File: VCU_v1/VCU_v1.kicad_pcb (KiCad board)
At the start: 4 copper layers, 265 parts, among them J1 Conn_01x04, J2 NUCLEO CONNECTOR LEFT, J3 NUCLEO CONNECTOR RIGHT, J4 Micro_SD_Card, J5 BRUHBus, J6 BRUHBus, J7 BRUHBus, J8 BRUHBus, Q1 PMOS, Q2 BSD235NH6327XT, Q3 SP8K80TB1, Q4 SP8K80TB1, Q5 SP8K80TB1, Q6 BSD235NH6327XT, SW1 SW_Push, U1 TPS5430, U10 TSB712AIDT, U11 MCP2562 E/SN, U12 MCP2562 E/SN, U13 TPA3116D2QDADRQ1, U14 PCM5102APWR, U2 TPS5430, U3 AMS1117-3.3, U4 MIC5200-4.8YS, U5 STM32H723ZGT6, U6 MX150 20-pin, U7 MX150 20-pin, U8 MX150 20-pin, U9 TSB712AIDT, Y1 16 MHz, Y2 32.768 kHz

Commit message: layout of power converters, connectors, nucleo headers
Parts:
- moved C14 289.5 mm to (341.1, 148.0)
- moved C15 289.5 mm to (341.1, 150.5)
- moved C16 289.5 mm to (341.1, 153.0)
- moved C17 289.5 mm to (341.1, 155.5)
- moved C26 289.5 mm to (441.7, 32.6)
- moved C27 289.5 mm to (441.7, 35.1)
- moved C28 289.5 mm to (441.7, 37.6)
- moved C29 289.5 mm to (441.7, 40.1)
- moved C30 289.5 mm to (441.7, 42.6)
- moved C31 289.5 mm to (441.7, 45.2)
- moved C32 289.5 mm to (441.7, 47.7)
- moved C33 289.5 mm to (441.7, 50.2)
- moved C45 289.5 mm to (353.8, 171.6)
- moved C46 289.5 mm to (353.8, 154.6)
- moved C55 289.5 mm to (468.7, 53.7)
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
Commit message: omids wisdom came all over my power converters
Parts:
- moved J7 420.7 mm to (34.0, 76.7), turned to 90 degrees
- moved J8 420.1 mm to (34.0, 98.0), turned to 90 degrees
- moved J4 367.5 mm to (32.1, 136.3), turned to 90 degrees
- moved U13 355.2 mm to (126.0, 71.3)
- moved U14 355.2 mm to (126.0, 87.4)
- moved H2 351.2 mm to (29.2, 57.1)
- moved L3 337.9 mm to (140.9, 74.5)
- moved L4 337.9 mm to (140.9, 88.2)
- moved H4 334.9 mm to (30.9, 170.7)
- moved U5 326.8 mm to (110.2, 138.0), turned to 90 degrees
- moved BT1 271.2 mm to (199.0, 147.1)
- moved TP1 196.9 mm to (212.5, 141.6)
- moved TP48 161.9 mm to (212.5, 137.4)
- moved H3 121.5 mm to (244.2, 168.5)
- moved L2 84.0 mm to (193.8, 118.9), turned to 0 degrees
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
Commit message: vcu placements complete
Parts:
- removed J5: BRUHBus, Connector_RJ:RJ45_Amphenol_RJHSE538X
- removed R33: 10k, Resistor_SMD:R_0603_1608Metric_Pad0.98x0.95mm_HandSolder
- removed R35: 100, Resistor_SMD:R_0603_1608Metric_Pad0.98x0.95mm_HandSolder
- removed R37, R39: 1.6k, Resistor_SMD:R_0603_1608Metric_Pad0.98x0.95mm_HandSolder
- D3, D4, D7: footprint LED_SMD:LED_0201_0603Metric_Pad0.64x0.40mm_HandSolder -> LED_SMD:LED_0603_1608Metric_Pad1.05x0.95mm_HandSolder
- U11, U12: value MCP2562 E/SN -> MCP2562FD-E/SN
- moved R79 431.7 mm to (43.7, 65.6), turned to -90 degrees
- moved R81 431.3 mm to (43.7, 76.5), turned to -90 degrees
- moved R80 430.5 mm to (43.7, 88.6), turned to -90 degrees
- moved R82 430.4 mm to (43.7, 98.0), turned to -90 degrees
- moved R78 424.0 mm to (47.2, 79.2), turned to 180 degrees
- moved R77 423.2 mm to (47.3, 86.4), turned to 180 degrees
- moved Q6 422.3 mm to (46.7, 82.8), turned to 90 degrees
- moved R10 421.0 mm to (37.8, 148.0), turned to -90 degrees
- moved R76 420.7 mm to (50.0, 80.1), turned to 90 degrees
- moved R75 420.2 mm to (50.0, 85.2), turned to -90 degrees
- moved C36 415.9 mm to (48.5, 154.8), turned to 90 degrees
- moved C32 412.4 mm to (42.2, 150.0)
- moved C37 411.8 mm to (52.1, 154.8), turned to 90 degrees
- moved C31 411.5 mm to (42.2, 143.6)
- moved C30 410.9 mm to (42.2, 138.5)
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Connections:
- Q2 pad 3: Net-(J6-CAN_IND) -> unconnected-(Q2B-D-Pad3)
- Q2 pad 4: GND -> unconnected-(Q2B-S-Pad4)
- Q2 pad 5: Net-(Q2B-G) -> unconnected-(Q2B-G-Pad5)
- Q2 pad 6: Net-(J5-CAN_IND) -> Net-(J6-CAN_IND)
- Q5 pad 1: /Connector-Root/BMS_FAULT- -> GND
- Q5 pad 3: /Connector-Root/IMD_FAULT- -> GND
- R36 pad 2: Net-(Q2B-G) -> Net-(Q2A-G)
- R60 pad 1: /Connector-Root/BMS_FAULT- -> GND
- R69 pad 1: /Connector-Root/IMD_FAULT- -> GND
- U6 pad 11: unconnected-(U6-Pad11) -> /BRUHbus/CAN1_L
- U6 pad 12: unconnected-(U6-Pad12) -> /BRUHbus/CAN1_H
- U6 pad 13: unconnected-(U6-Pad13) -> /Connector-Root/RTD_BTN+
- U6 pad 14: unconnected-(U6-Pad14) -> /Connector-Root/RTD_BTN-
- U6 pad 15: unconnected-(U6-Pad15) -> /Connector-Root/PRECHARGE_BTN+
- U6 pad 16: unconnected-(U6-Pad16) -> /Connector-Root/PRECHARGE_BTN-
- U7 pad 1: /Connector-Root/SPEAKER+ -> /STM32-Root/STM32H723ZGT6/PG4
- U7 pad 10: /Connector-Root/BMS-FAULT -> /Connector-Root/SPEAKER+
- U7 pad 11: /Connector-Root/SPEAKER- -> /STM32-Root/STM32H723ZGT6/PB15
- U7 pad 2: /STM32-Root/STM32H723ZGT6/PB15 -> /STM32-Root/STM32H723ZGT6/PG5
- U7 pad 3: /STM32-Root/STM32H723ZGT6/PG4 -> /STM32-Root/STM32H723ZGT6/PG6
- U7 pad 4: /STM32-Root/STM32H723ZGT6/PG5 -> /STM32-Root/STM32H723ZGT6/PG7
- U7 pad 5: /STM32-Root/STM32H723ZGT6/PG6 -> /STM32-Root/STM32H723ZGT6/PG8
- U7 pad 6: /STM32-Root/STM32H723ZGT6/PG7 -> /Connector-Root/BSPD-FAULT
- U7 pad 7: /STM32-Root/STM32H723ZGT6/PG8 -> /Connector-Root/IMD-FAULT
- U7 pad 8: /Connector-Root/BSPD-FAULT -> /Connector-Root/BMS-FAULT
- U7 pad 9: /Connector-Root/IMD-FAULT -> /Connector-Root/SPEAKER-
- U8 pad 1: /Connector-Root/PRECHARGE_BTN+ -> unconnected-(U8-Pad1)
- U8 pad 11: /Connector-Root/PRECHARGE_BTN- -> unconnected-(U8-Pad11)
- U8 pad 12: /Connector-Root/RTD_BTN- -> unconnected-(U8-Pad12)
- U8 pad 19: /Connector-Root/IMD_FAULT- -> GND
- U8 pad 2: /Connector-Root/RTD_BTN+ -> unconnected-(U8-Pad2)
- U8 pad 20: /Connector-Root/BMS_FAULT- -> GND
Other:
- board outline added: 42.8 x 2.8 mm

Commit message: ok real placements, will begin routing now but will prolly revert to this commit ngl
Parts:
- removed U13: TPA3116D2QDADRQ1, TPA3116D2QDADRQ1:Untitled
- moved H1 26.6 mm to (237.5, 68.6)
- moved TP10 20.6 mm to (78.7, 65.8)
- moved BT1 13.9 mm to (109.2, 142.3), turned to 0 degrees
- moved U8 12.7 mm to (225.2, 60.6)
- moved C83 11.4 mm to (218.2, 71.9)
- moved C84 11.4 mm to (205.2, 72.1)
- moved D3 11.4 mm to (238.0, 101.9)
- moved D4 11.4 mm to (237.9, 107.7)
- moved D7 11.4 mm to (238.2, 95.2)
- moved R12 11.4 mm to (233.8, 95.2)
- moved R57 11.4 mm to (201.2, 71.4)
- moved R60 11.4 mm to (188.2, 78.0)
- moved R62 11.4 mm to (191.5, 79.0)
- moved R65 11.4 mm to (191.5, 68.1)
- moved R66 11.4 mm to (221.8, 73.2)
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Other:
- board size 42.8 x 2.8 mm -> 217.4 x 125 mm

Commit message: i lied i had to add gnd test points
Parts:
- added TP49: RH-5015, TestPoint:TestPoint_Keystone_5015_Micro_Mini, F.Cu at (205.1, 137.9)
- added TP50: RH-5015, TestPoint:TestPoint_Keystone_5015_Micro_Mini, F.Cu at (219.2, 156.4)
- added TP51: RH-5015, TestPoint:TestPoint_Keystone_5015_Micro_Mini, F.Cu at (212.1, 66.0)
- added TP52: RH-5015, TestPoint:TestPoint_Keystone_5015_Micro_Mini, F.Cu at (56.9, 83.4)
- added TP53: RH-5015, TestPoint:TestPoint_Keystone_5015_Micro_Mini, F.Cu at (52.6, 109.2)
- added TP54: RH-5015, TestPoint:TestPoint_Keystone_5015_Micro_Mini, F.Cu at (67.9, 95.4)
- added TP55: RH-5015, TestPoint:TestPoint_Keystone_5015_Micro_Mini, F.Cu at (89.6, 81.3)
- added TP56: RH-5015, TestPoint:TestPoint_Keystone_5015_Micro_Mini, F.Cu at (238.8, 82.1)
- added TP57: RH-5015, TestPoint:TestPoint_Keystone_5015_Micro_Mini, F.Cu at (238.8, 86.9)
- added TP58: RH-5015, TestPoint:TestPoint_Keystone_5015_Micro_Mini, F.Cu at (238.8, 91.6)
- added TP59: RH-5015, TestPoint:TestPoint_Keystone_5015_Micro_Mini, F.Cu at (238.8, 96.4)
- added U13: TPA3116D2QDADRQ1, TPA3116D2QDADRQ1:Untitled, F.Cu at (120.0, 89.6)
- moved TP5 13.6 mm to (219.2, 151.8)
- moved D3 6.46 mm to (238.9, 108.3)
- moved D4 6.46 mm to (238.7, 114.1)
- moved D7 6.46 mm to (239.0, 101.7)
- moved R12 6.46 mm to (234.7, 101.7)
- moved R7 6.46 mm to (234.7, 108.3)
- moved R8 6.46 mm to (234.7, 114.1)
- moved TP39 1.53 mm to (207.1, 66.0)
- moved TP41 1.53 mm to (202.1, 66.0)
- moved TP40 1.53 mm to (197.0, 66.0)
- moved TP2 0.52 mm to (205.1, 134.7)

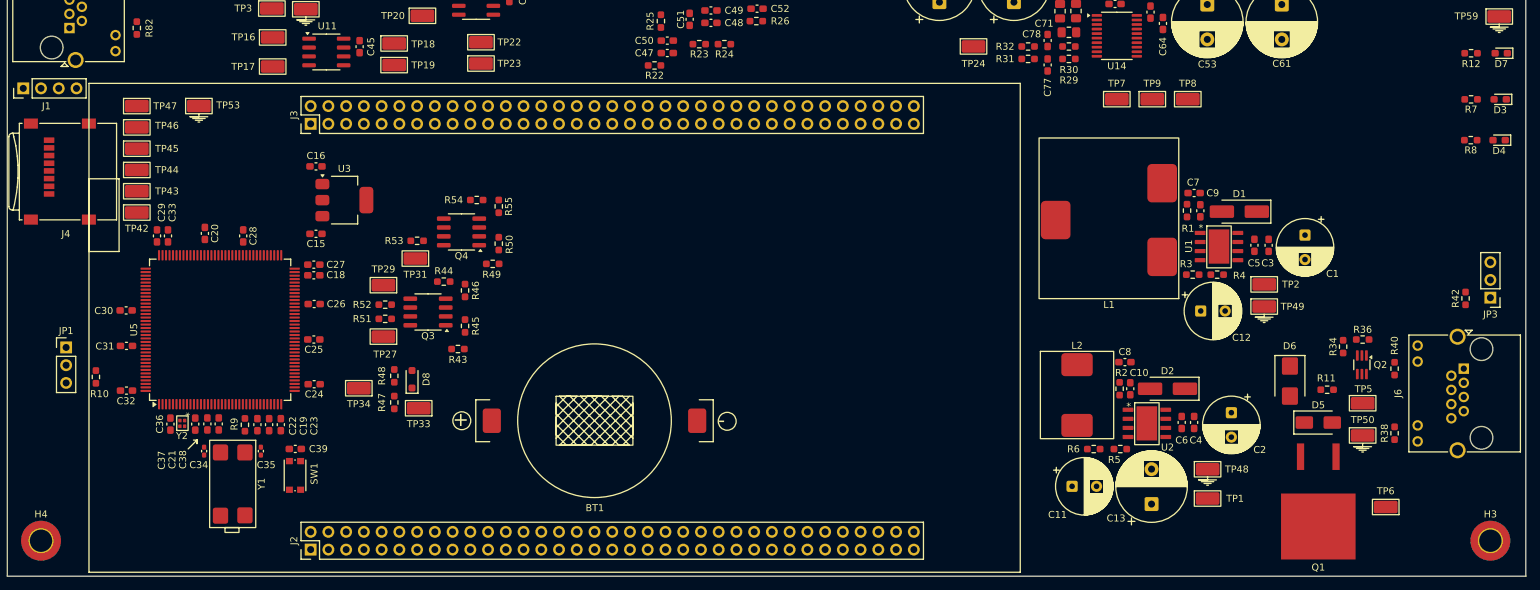
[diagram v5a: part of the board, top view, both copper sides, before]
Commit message: stm power routing complete, power polygons done
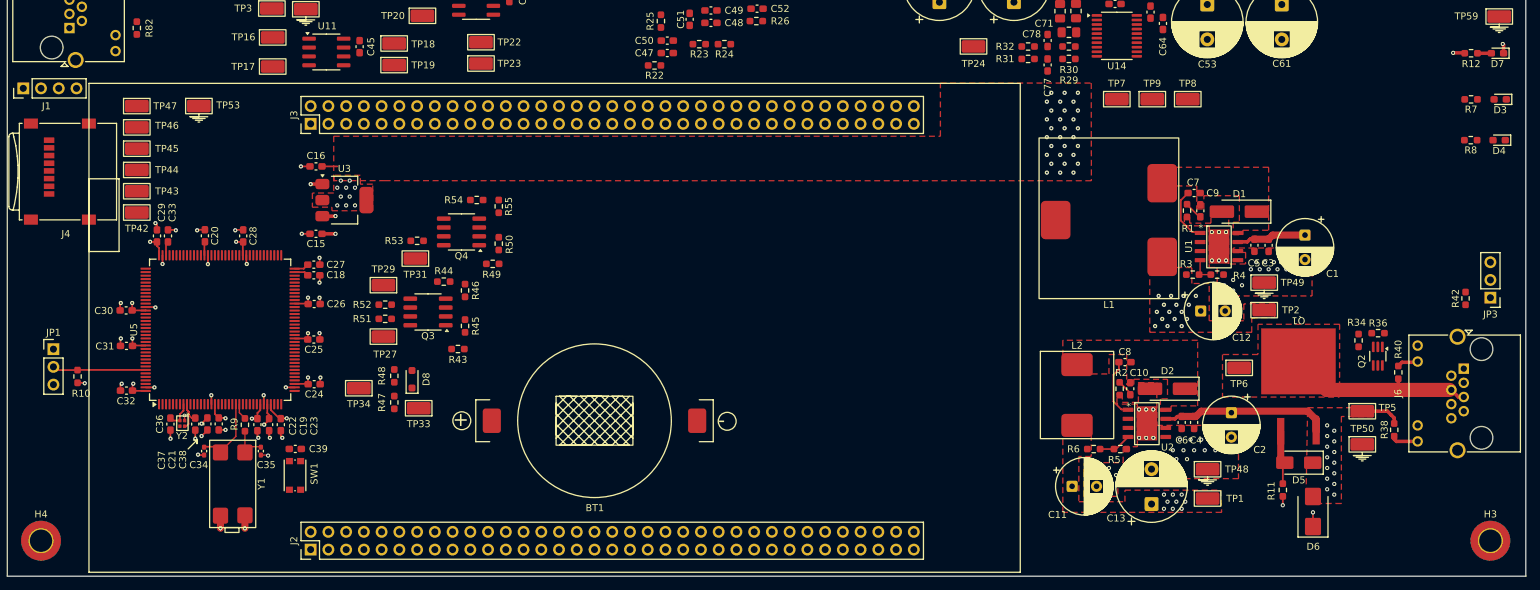
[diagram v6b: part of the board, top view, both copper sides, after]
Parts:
- moved Q1 35.8 mm to (210.0, 139.8), turned to 0 degrees
- moved TP6 28.9 mm to (201.5, 146.7), turned to 0 degrees
- moved D6 19.0 mm to (212.1, 167.3), turned to 90 degrees
- moved R11 15.7 mm to (207.8, 164.2), turned to -90 degrees
- moved D5 6.39 mm to (210.1, 160.3), turned to 180 degrees
- moved TP2 3.68 mm to (205.1, 138.4)
- moved TP49 3.43 mm to (205.1, 134.5)
- moved R10 2.63 mm to (35.2, 147.9)
- moved Q2 2.60 mm to (221.4, 145.0)
- moved R36 2.39 mm to (221.4, 141.7)
- moved R34 2.38 mm to (218.6, 142.8)
- moved JP1 1.83 mm to (31.8, 144.0)
- moved TP50 1.27 mm to (219.2, 157.7)
- moved TP5 1.14 mm to (219.2, 152.9)
- moved R40 0.75 mm to (224.3, 147.3)
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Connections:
- C81 pad 1: 3.3V -> +3.3V
- C82 pad 1: 3.3V -> +3.3V
- C83 pad 1: 3.3V -> +3.3V
- C84 pad 1: 3.3V -> +3.3V
- J6 pad SH: GND -> unconnected-(J6-SHIELD-PadSH)
- J7 pad SH: GND -> unconnected-(J7-SHIELD-PadSH)
- J8 pad SH: GND -> unconnected-(J8-SHIELD-PadSH)
- R58 pad 1: 3.3V -> +3.3V
- R63 pad 1: 3.3V -> +3.3V
- R67 pad 1: 3.3V -> +3.3V
- R73 pad 1: 3.3V -> +3.3V
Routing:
- net GND: track 0.00 -> 45.9 mm, vias 0 -> 85
- net +3.3V: track 0.00 -> 45.2 mm, vias 0 -> 54
- net +24V: track 0.00 -> 43.8 mm, vias 0 -> 15
- net /BRUHbus/Vin: track 0.00 -> 34.2 mm
- net Net-(JP1-C): track 0.00 -> 13.4 mm
- net Net-(U5B-PH0-OSC_IN): track 0.00 -> 10.5 mm
- net Net-(U2-BOOT): track 0.00 -> 8.54 mm
- net Net-(U1-BOOT): track 0.00 -> 7.90 mm
- net Net-(D5-A): track 0.00 -> 7.87 mm
- net Net-(C35-Pad1): track 0.00 -> 5.59 mm
- net Net-(U5B-PC15-OSC32_OUT): track 0.00 -> 5.24 mm
- net Net-(U2-VSENSE): track 0.00 -> 4.71 mm
- net Net-(U5B-PC14-OSC32_IN): track 0.00 -> 4.06 mm
- net Net-(J6-CAN_IND): track 0.00 -> 3.92 mm
- net +5V: track 0.00 -> 3.82 mm, vias 0 -> 11
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- added copper zone on F.Cu, net +24V
- added copper zone on In2.Cu, net +24V
- added copper zone on F.Cu, net +3.3V
- added copper zone on In2.Cu, net +3.3V
- added copper zone on F.Cu, net +5V
- added copper zone on In2.Cu, net +5V
- added copper zone on F.Cu, net /BRUHbus/Vin
- added copper zone on F.Cu, net 20V-AMP
- added copper zone on In2.Cu, net 20V-AMP
- added copper zone on F.Cu, net GND
- added copper zone on In1.Cu, net GND
- added copper zone on F.Cu, net Net-(D1-K)
- added copper zone on F.Cu, net Net-(D2-K)
